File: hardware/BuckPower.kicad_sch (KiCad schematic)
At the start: 29 parts, among them Q401 2N7002NXAKR, U401 SIC437A

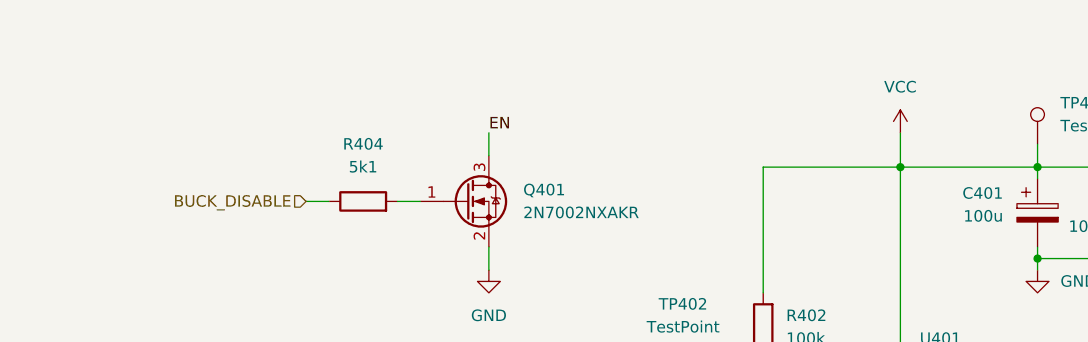
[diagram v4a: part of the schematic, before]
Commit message: Global labels, explanation texts, fix spring connector
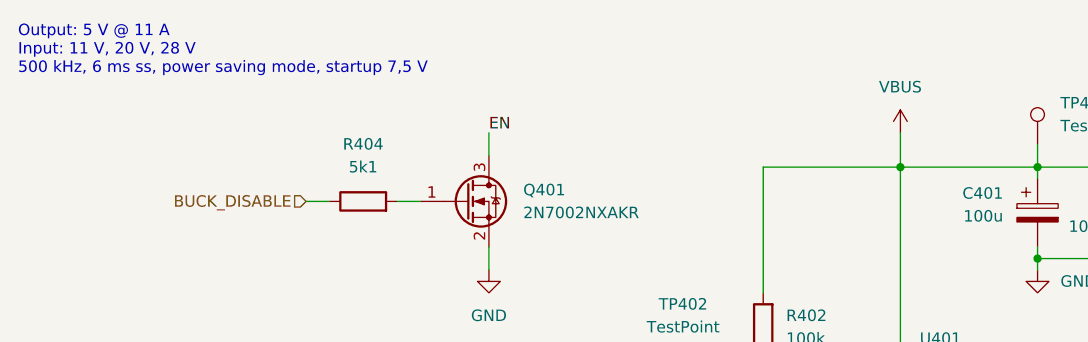
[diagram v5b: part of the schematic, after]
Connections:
- net VCC renamed VBUS
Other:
- note added: "Output: 5 V @ 11 A Input: 11 V, 20 V, 28 V 500 kHz, 6 ms ss, power saving mode, startup 7,5 V"
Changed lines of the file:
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@@
 		(title "Glowbuck")
 	)
+	(text "Output: 5 V @ 11 A\nInput: 11 V, 20 V, 28 V\n500 kHz, 6 ms ss, power saving mode, startup 7,5 V"
+		(exclude_from_sim no)
+		(at 14.986 14.732 0)
+		(effects
+			(font
+				(size 1.27 1.27)
+			)
+			(justify left top)
+		)
+	)
 	(junction
 		(at 148.59 81.28)
@@
 	)
 	(symbol
-		(lib_id "power:VCC")
-		(at 113.03 26.67 0)
-		(unit 1)
-		(exclude_from_sim no)
-		(in_bom yes)
-		(on_board yes)
-		(dnp no)
-		(fields_autoplaced yes)
-		(property "Reference" "#PWR0401"
-			(at 113.03 30.48 0)
-			(effects
-				(font
-					(size 1.27 1.27)
-				)
-				(hide yes)
-			)
-		)
-		(property "Value" "VCC"
-			(at 113.03 21.59 0)
-			(effects
-				(font
-					(size 1.27 1.27)
-				)
-			)
-		)
-		(property "Footprint" ""
-			(at 113.03 26.67 0)
-			(effects
-				(font
-					(size 1.27 1.27)
-				)
-				(hide yes)
-			)
-		)
-		(property "Datasheet" ""
-			(at 113.03 26.67 0)
-			(effects
-				(font
-					(size 1.27 1.27)
-				)
-				(hide yes)
-			)
-		)
-		(property "Description" "Power symbol creates a global label with name \"VCC\""
-			(at 113.03 26.67 0)
-			(effects
-				(font
-					(size 1.27 1.27)
-				)
-				(hide yes)
-			)
-		)
-		(pin "1"
-		)
-		(instances
-			(project "glowbuck"
-				(path "/5c22e6dd-0c33-4422-b6db-bb3ef40a8534/015535ff-5c39-4e5a-877e-d1b03c5377a0"
-					(reference "#PWR0401")
-					(unit 1)
-				)
-			)
-		)
-	)
-	(symbol
 		(lib_id "Device:C")
 		(at 176.53 72.39 0)
@@
 					(unit 1)
 				)
+			)
+		)
+	)
+	(symbol
+		(lib_id "power:VBUS")
+		(at 113.03 26.67 0)
+		(unit 1)
+		(exclude_from_sim no)
+		(in_bom yes)
+		(on_board yes)
+		(dnp no)
+		(fields_autoplaced yes)
+		(property "Reference" "#PWR0401"
+			(at 113.03 30.48 0)
+			(effects
+				(font
+					(size 1.27 1.27)
+				)
+				(hide yes)
+			)
+		)
+		(property "Value" "VBUS"
+			(at 113.03 21.59 0)
+			(effects
+				(font
+					(size 1.27 1.27)
+				)
+			)
+		)
+		(property "Footprint" ""
+			(at 113.03 26.67 0)
+			(effects
+				(font
+					(size 1.27 1.27)
+				)
+				(hide yes)
+			)
+		)
+		(property "Datasheet" ""
+			(at 113.03 26.67 0)
+			(effects
+				(font
+					(size 1.27 1.27)
+				)
+				(hide yes)
+			)
+		)
+		(property "Description" "Power symbol creates a global label with name \"VBUS\""
+			(at 113.03 26.67 0)
+			(effects
+				(font
+					(size 1.27 1.27)
+				)
+				(hide yes)
+			)
+		)
+		(pin "1"
+		)
+		(instances
+			(project ""
+				(path "/5c22e6dd-0c33-4422-b6db-bb3ef40a8534/015535ff-5c39-4e5a-877e-d1b03c5377a0"
+					(reference "#PWR0401")
+					(unit 1)
+				)

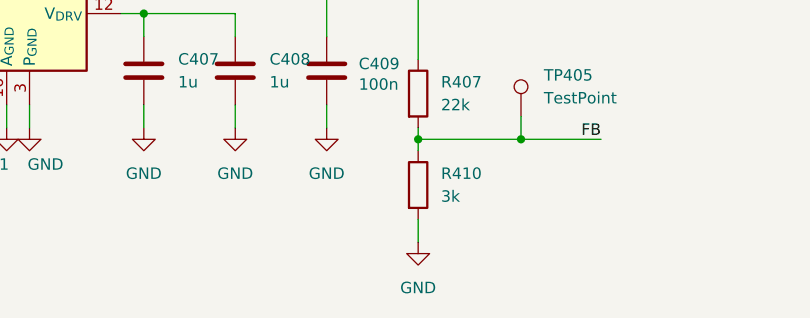
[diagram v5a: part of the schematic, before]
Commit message: Layout Stecker final, USB done, buck wip
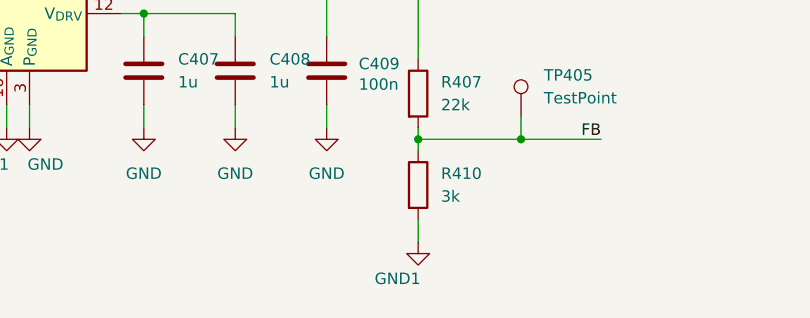
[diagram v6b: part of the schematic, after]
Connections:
- net GND: no longer R410.2
- net GND1: now also R410.2

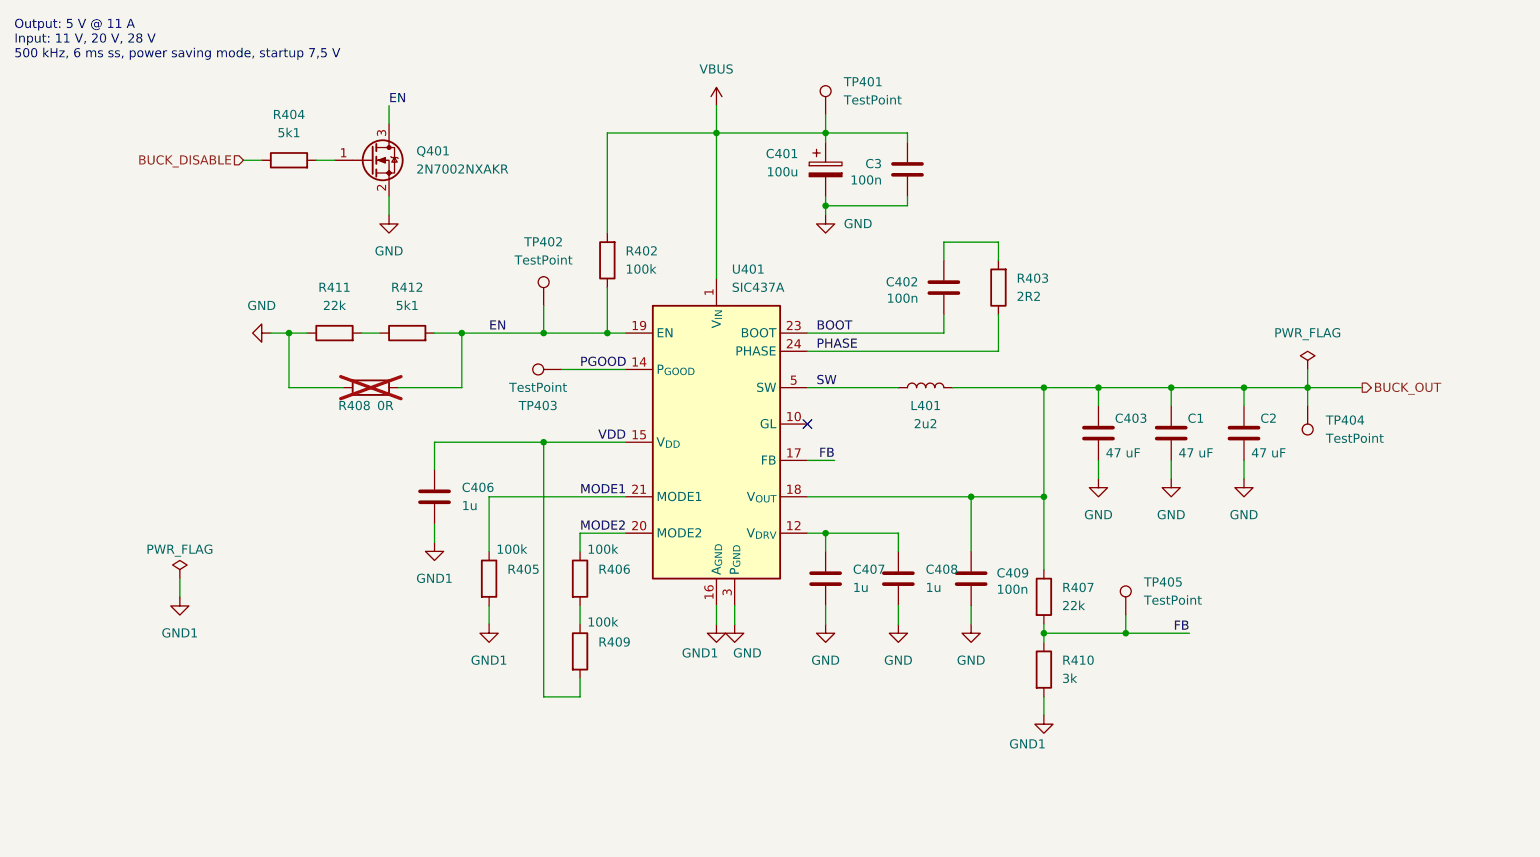
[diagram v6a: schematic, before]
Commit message: Layout in progress. I2C done
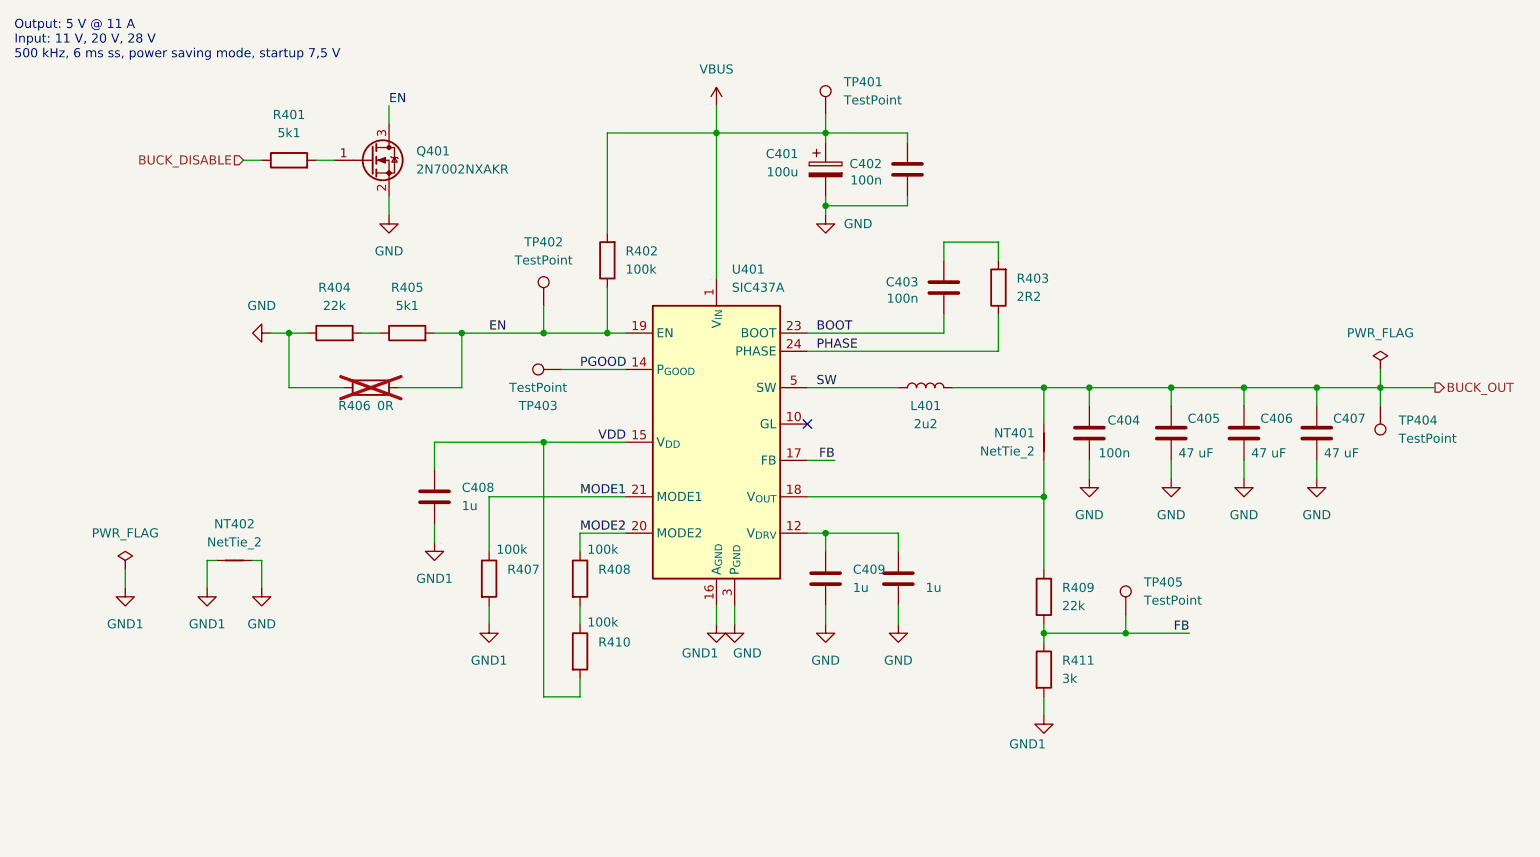
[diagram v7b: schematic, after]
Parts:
- added NT401: NetTie_2, glowbuck:NETTIE_0.2mm, symbol Device:NetTie_2
- added NT402: NetTie_2, glowbuck:NETTIE_0.3mm, symbol Device:NetTie_2
- renumbered C3 to C402, C402 to C403, C409 to C404, C403 to C405, C1 to C406, C2 to C407, C406 to C408, C407 to C409, C408 to C410, R404 to R401, R411 to R404, R412 to R405, R408 to R406, R405 to R407, R406 to R408, R407 to R409, R409 to R410, R410 to R411
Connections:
- net BUCK_OUT: now also NT401.1; no longer R409.1, U401.18 (V_{OUT})
- net GND: now also NT402.2
- net GND1: now also NT402.1
- new net: NT401.2, R409.1, U401.18 (V_{OUT})
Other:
- moved on the sheet: C404, C405, C406, C407, TP404

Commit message: Added ManufacturerNumber for every item and fixed bom errors
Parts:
- C401: ManufacturerNumber (none) -> PCZ1V101MCL6GS
- C402, C403, C404: ManufacturerNumber (none) -> CL10B104KB8WPND
- C405, C406, C407: MouserNumber (none) -> 81-GRM32ER71A476KE5L
- C408, C410: ManufacturerNumber (none) -> CL10B105KA8NFNC; MouserNumber (none) -> 187-CL10B105KA8NFNC
- C409: ManufacturerNumber (none) -> CL10B105KA8NFNC; MouserNumber 187-CL10B104KB8WPND -> 187-CL10B105KA8NFNC
- Q401: ManufacturerNumber (none) -> 2N7002NXAKR
- R401, R405: ManufacturerNumber (none) -> RT0603DRE075K11L; MouserNumber 652-CRT0603FZ1002ELF -> 603-RT0603DRE075K11L; now in the parts list
- R402, R407, R408, R410: ManufacturerNumber (none) -> RT0603FRE07100KL; MouserNumber (none) -> 603-RT0603FRE07100KL
- R403: ManufacturerNumber (none) -> CRCW06032R20FKEA; MouserNumber (none) -> 71-CRCW0603-2.2-E3
- R404, R409: ManufacturerNumber (none) -> RT0603DRE0722KL; MouserNumber (none) -> 603-RT0603DRE0722KL
- R406: ManufacturerNumber (none) -> RC0603FR-130RL
- R411: ManufacturerNumber (none) -> RC0603FR-133KL; MouserNumber (none) -> 603-RC0603FR-133KL
- U401: ManufacturerNumber (none) -> SIC437AED-T1-GE3; MouserNumber (none) -> 78-SIC437AED-T1-GE3
